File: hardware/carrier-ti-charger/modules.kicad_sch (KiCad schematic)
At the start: 30 parts, among them J10 J_ADS_MAIN ADSBee J5, J11 J_ADS_GNSS ADSBee J4, J6 J_ESP_A support, J7 J_ESP_B power/UART, J8 J_ESP_C I2C, J9 J_ESP_D support, U11 TPS259474LRPWR, U12 TPS259474LRPWR

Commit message: Consolidate bom.
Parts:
- C38, C39: value 100n 50V -> 100n 16V; footprint Capacitor_SMD:C_0603_1608Metric -> carrier:C_0402_1005Metric_NoSilk; LCSC C14663 -> C1525; MPN (none) -> CL05B104KO5NNNC
- R73, R75: value 5.36k -> 5.6k 1%; LCSC C2924137 -> C23189; MPN AR03BTCX5361A -> 0603WAF5601T5E; TCR 25 ppm/C -> 100 ppm/C; Tolerance 0.1% -> 1%
- R74, R76: value 1.5k -> 1.5k 1%; LCSC C281775 -> C25867; MPN RT0402BRD071K5L -> 0402WGF1501TCE; TCR 25 ppm/C -> 100 ppm/C; Tolerance 0.1% -> 1%
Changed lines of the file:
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@@
 			)
 		)
-		(property "Value" "1.5k"
+		(property "Value" "1.5k 1%"
 			(at 52.07 148.59 0)
 			(show_name no)
@@
 			)
 		)
-		(property "Description" "OVLO divider, 0.1%, 25 ppm/C, 62.5 mW, 50 V"
+		(property "Description" "OVLO divider bottom, U11, 1%, 100 ppm/C"
 			(at 54.61 147.32 0)
 			(hide yes)
@@
 			)
 		)
-		(property "LCSC" "C281775"
+		(property "LCSC" "C25867"
 			(at 54.61 147.32 0)
 			(hide yes)
@@
 			)
 		)
-		(property "MPN" "RT0402BRD071K5L"
+		(property "MPN" "0402WGF1501TCE"
 			(at 54.61 147.32 0)
 			(hide yes)
@@
 			)
 		)
-		(property "Tolerance" "0.1%"
+		(property "Tolerance" "1%"
 			(at 54.61 147.32 0)
 			(hide yes)
@@
 			)
 		)
-		(property "TCR" "25 ppm/C"
+		(property "TCR" "100 ppm/C"
 			(at 54.61 147.32 0)
 			(hide yes)
@@
 			)
 		)
-		(property "Value" "100n 50V"
+		(property "Value" "100n 16V"
 			(at 29.21 57.15 0)
 			(show_name no)
@@
 			)
 		)
-		(property "Footprint" "Capacitor_SMD:C_0603_1608Metric"
+		(property "Footprint" "carrier:C_0402_1005Metric_NoSilk"
 			(at 26.67 55.88 0)
 			(hide yes)
@@
 			)
 		)
-		(property "LCSC" "C14663"
+		(property "LCSC" "C1525"
+			(at 26.67 55.88 0)
+			(hide yes)
+			(show_name no)
+			(do_not_autoplace no)
+			(effects
+				(font
+					(size 1.27 1.27)
+				)
+			)
+		)
+		(property "MPN" "CL05B104KO5NNNC"
 			(at 26.67 55.88 0)
 			(hide yes)
@@
 			)
 		)
-		(property "Value" "5.36k"
+		(property "Value" "5.6k 1%"
 			(at 52.07 80.01 0)
 			(show_name no)
@@
 			)
 		)
-		(property "Description" "OVLO divider, 0.1%, 25 ppm/C, 100 mW, 75 V"
+		(property "Description" "OVLO divider top, U12, 1%, 100 ppm/C"
 			(at 54.61 78.74 0)
 			(hide yes)
@@
 			)
 		)
-		(property "LCSC" "C2924137"
+		(property "LCSC" "C23189"
 			(at 54.61 78.74 0)
 			(hide yes)
@@
 			)
 		)
-		(property "MPN" "AR03BTCX5361A"
+		(property "MPN" "0603WAF5601T5E"
 			(at 54.61 78.74 0)
 			(hide yes)
@@
 			)
 		)
-		(property "Tolerance" "0.1%"
+		(property "Tolerance" "1%"
 			(at 54.61 78.74 0)
 			(hide yes)
@@
 			)
 		)
-		(property "TCR" "25 ppm/C"
+		(property "TCR" "100 ppm/C"
 			(at 54.61 78.74 0)
 			(hide yes)
@@
 			)
 		)
-		(property "Value" "1.5k"
+		(property "Value" "1.5k 1%"
 			(at 52.07 87.63 0)
 			(show_name no)
@@
 			)
 		)
-		(property "Description" "OVLO divider, 0.1%, 25 ppm/C, 62.5 mW, 50 V"
+		(property "Description" "OVLO divider bottom, U12, 1%, 100 ppm/C"
 			(at 54.61 86.36 0)
 			(hide yes)
@@
 			)
 		)
-		(property "LCSC" "C281775"
+		(property "LCSC" "C25867"
 			(at 54.61 86.36 0)
 			(hide yes)
@@
 			)
 		)
-		(property "MPN" "RT0402BRD071K5L"
+		(property "MPN" "0402WGF1501TCE"
 			(at 54.61 86.36 0)
 			(hide yes)
@@
 			)
 		)
-		(property "Tolerance" "0.1%"
+		(property "Tolerance" "1%"
 			(at 54.61 86.36 0)
 			(hide yes)
@@
 			)
 		)
-		(property "TCR" "25 ppm/C"
+		(property "TCR" "100 ppm/C"
 			(at 54.61 86.36 0)
 			(hide yes)
@@
 			)
 		)
-		(property "Value" "100n 50V"
+		(property "Value" "100n 16V"
 			(at 29.21 118.11 0)
 			(show_name no)
@@
 			)
 		)
-		(property "Footprint" "Capacitor_SMD:C_0603_1608Metric"
+		(property "Footprint" "carrier:C_0402_1005Metric_NoSilk"
 			(at 26.67 116.84 0)
 			(hide yes)
@@
 			)
 		)
-		(property "LCSC" "C14663"
+		(property "LCSC" "C1525"
+			(at 26.67 116.84 0)
+			(hide yes)
+			(show_name no)
+			(do_not_autoplace no)
+			(effects
+				(font
+					(size 1.27 1.27)
+				)
+			)
+		)
+		(property "MPN" "CL05B104KO5NNNC"
 			(at 26.67 116.84 0)
 			(hide yes)
@@
 			)
 		)
-		(property "Value" "5.36k"
+		(property "Value" "5.6k 1%"
 			(at 52.07 140.97 0)
 			(show_name no)
@@
 			)
 		)
-		(property "Description" "OVLO divider, 0.1%, 25 ppm/C, 100 mW, 75 V"
+		(property "Description" "OVLO divider top, U11, 1%, 100 ppm/C"
 			(at 54.61 139.7 0)
 			(hide yes)
@@
 			)
 		)
-		(property "LCSC" "C2924137"
+		(property "LCSC" "C23189"
 			(at 54.61 139.7 0)
 			(hide yes)
@@
 			)
 		)
-		(property "MPN" "AR03BTCX5361A"
+		(property "MPN" "0603WAF5601T5E"
 			(at 54.61 139.7 0)
 			(hide yes)
@@
 			)
 		)
-		(property "Tolerance" "0.1%"
+		(property "Tolerance" "1%"
 			(at 54.61 139.7 0)
 			(hide yes)
@@
 			)
 		)
-		(property "TCR" "25 ppm/C"
+		(property "TCR" "100 ppm/C"
 			(at 54.61 139.7 0)
 			(hide yes)

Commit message: Polishing.
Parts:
- added J2: XIAO Plus power/UART/PWM, Connector_PinHeader_2.54mm:PinHeader_1x07_P2.54mm_Vertical, symbol Connector_Generic:Conn_01x07
- added J3: XIAO Plus I2C/spares, Connector_PinHeader_2.54mm:PinHeader_1x07_P2.54mm_Vertical, symbol Connector_Generic:Conn_01x07
- renumbered J7 to J1, J6 to J4, J11 to J5, J10 to J6, J9 to J8, J8 to J9, JP2 to JP3
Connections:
- net +ESP_3V3: now also J2.3 (Pin_3)
- net +ESP_5V: now also J2.1 (Pin_1)
- net BUZZ_PWM: now also J2.5 (Pin_5)
- net ESP_UART_RX: now also J2.6 (Pin_6)
- net ESP_UART_TX: now also J2.7 (Pin_7)
- net GND: now also J2.2 (Pin_2); no longer J1.4 (Pin_4), J4.4 (Pin_4)
- net I2C_SCL: now also J3.6 (Pin_6)
- net I2C_SDA: now also J3.5 (Pin_5)
- net XIAO_D0: now reaches J4.1 (Pin_1)
- net XIAO_D0: now also J3.1 (Pin_1)
- net XIAO_D1: now reaches J4.2 (Pin_2)
- net XIAO_D1: now also J3.2 (Pin_2)
- net XIAO_D2: now reaches J4.3 (Pin_3)
- net XIAO_D2: now also J3.3 (Pin_3)
- net XIAO_D6: now reaches J4.7 (Pin_7)
- net XIAO_D6: now also J3.7 (Pin_7)
- new net XIAO_D10: J1.4 (Pin_4), J2.4 (Pin_4)
- new net XIAO_D3: J3.4 (Pin_4), J4.4 (Pin_4)
- no-connect marks 21 -> 17

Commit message: Polishing.
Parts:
- R70, R71: value 1.65k -> 1.8k; LCSC C22845 -> C4177; MPN 0603WAF1651T5E -> 0603WAF1801T5E; Manufacturer (none) -> UNI-ROYAL; TCR (none) -> 100 ppm/°C; Tolerance (none) -> 1%
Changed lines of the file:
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@@
 			)
 		)
-		(property "Value" "1.65k"
+		(property "Value" "1.8k"
 			(at 67.31 148.59 0)
 			(show_name no)
@@
 			)
 		)
-		(property "Datasheet" ""
+		(property "Datasheet" "https://www.uni-royal.cn/en/images/userfile/file/1753752986c56505e6d9ab55c7.pdf"
 			(at 69.85 147.32 0)
 			(hide yes)
@@
 			)
 		)
-		(property "LCSC" "C22845"
-			(at 69.85 147.32 0)
-			(hide yes)
-			(show_name no)
-			(do_not_autoplace no)
-			(effects
-				(font
-					(size 1.27 1.27)
-				)
-			)
-		)
-		(property "MPN" "0603WAF1651T5E"
+		(property "LCSC" "C4177"
+			(at 69.85 147.32 0)
+			(hide yes)
+			(show_name no)
+			(do_not_autoplace no)
+			(effects
+				(font
+					(size 1.27 1.27)
+				)
+			)
+		)
+		(property "TCR" "100 ppm/°C"
+			(at 69.85 147.32 0)
+			(hide yes)
+			(show_name no)
+			(do_not_autoplace no)
+			(effects
+				(font
+					(size 1.27 1.27)
+				)
+			)
+		)
+		(property "Tolerance" "1%"
+			(at 69.85 147.32 0)
+			(hide yes)
+			(show_name no)
+			(do_not_autoplace no)
+			(effects
+				(font
+					(size 1.27 1.27)
+				)
+			)
+		)
+		(property "Manufacturer" "UNI-ROYAL"
+			(at 69.85 147.32 0)
+			(hide yes)
+			(show_name no)
+			(do_not_autoplace no)
+			(effects
+				(font
+					(size 1.27 1.27)
+				)
+			)
+		)
+		(property "MPN" "0603WAF1801T5E"
 			(at 69.85 147.32 0)
 			(hide yes)
@@
 			)
 		)
-		(property "Value" "1.65k"
+		(property "Value" "1.8k"
 			(at 67.31 87.63 0)
 			(show_name no)
@@
 			)
 		)
-		(property "Datasheet" ""
+		(property "Datasheet" "https://www.uni-royal.cn/en/images/userfile/file/1753752986c56505e6d9ab55c7.pdf"
 			(at 69.85 86.36 0)
 			(hide yes)
@@
 			)
 		)
-		(property "LCSC" "C22845"
-			(at 69.85 86.36 0)
-			(hide yes)
-			(show_name no)
-			(do_not_autoplace no)
-			(effects
-				(font
-					(size 1.27 1.27)
-				)
-			)
-		)
-		(property "MPN" "0603WAF1651T5E"
-			(at 69.85 86.36 0)
-			(hide yes)
+		(property "LCSC" "C4177"
+			(at 69.85 86.36 0)
+			(hide yes)
+			(show_name no)
+			(do_not_autoplace no)
+			(effects
+				(font
+					(size 1.27 1.27)
+				)
+			)
+		)
+		(property "TCR" "100 ppm/°C"
+			(at 69.85 86.36 0)
+			(hide yes)
+			(show_name no)
+			(do_not_autoplace no)
+			(effects
+				(font
+					(size 1.27 1.27)
+				)
+			)
+		)
+		(property "Tolerance" "1%"
+			(at 69.85 86.36 0)
+			(hide yes)
+			(show_name no)
+			(do_not_autoplace no)
+			(effects
+				(font
+					(size 1.27 1.27)
+				)
+			)
+		)
+		(property "Manufacturer" "UNI-ROYAL"
+			(at 69.85 86.36 0)
+			(hide yes)
+			(show_name no)
+			(do_not_autoplace no)
+			(effects
+				(font
+					(size 1.27 1.27)
+				)
+			)
+		)
+		(property "MPN" "0603WAF1801T5E"
+			(at 69.85 86.36 0)
+			(hide yes)

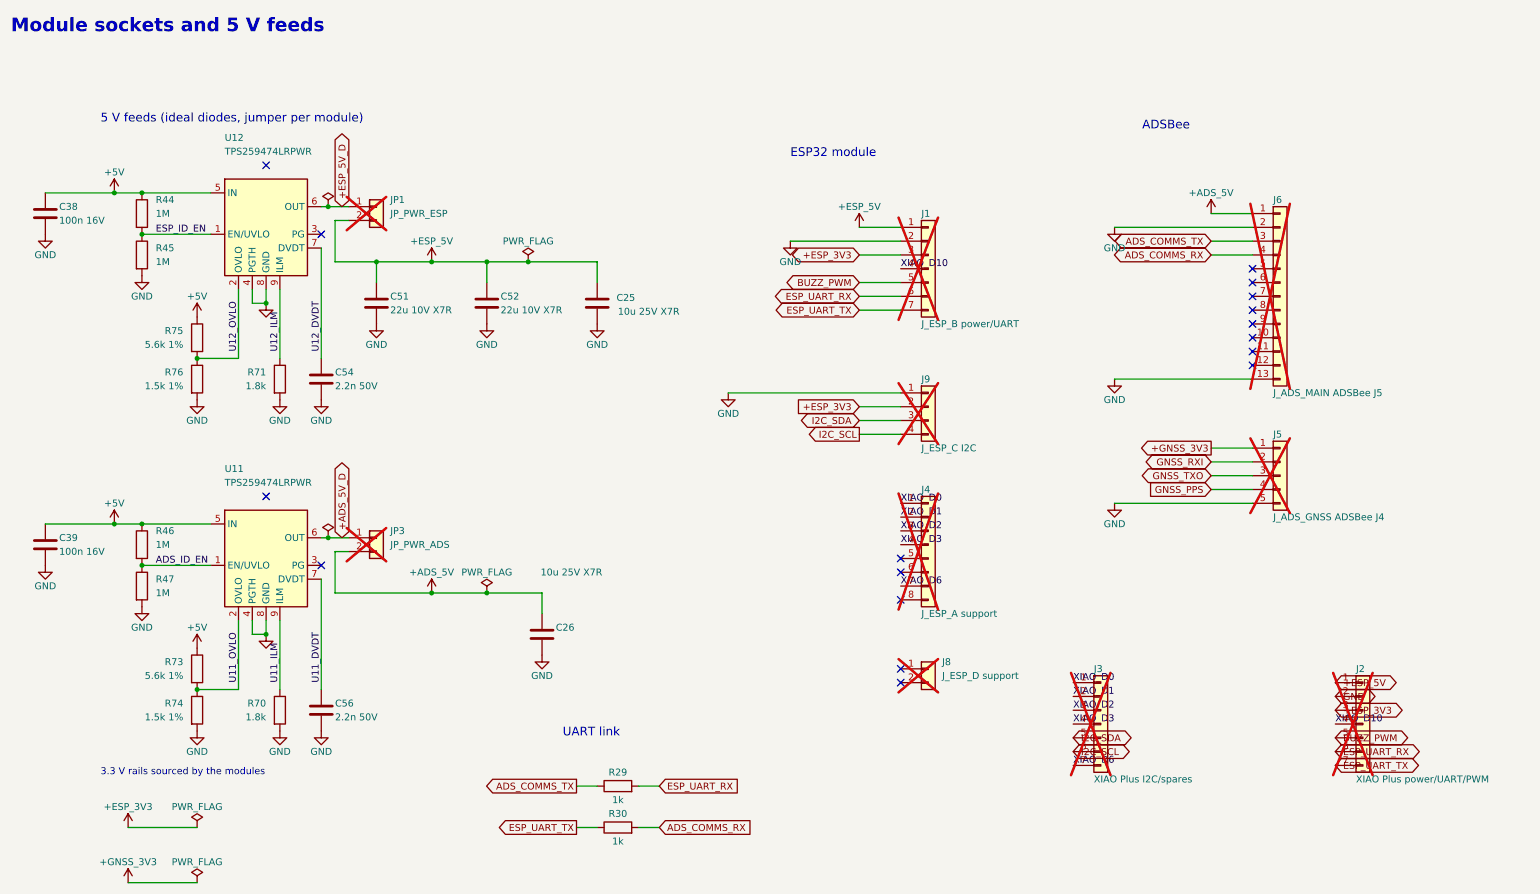
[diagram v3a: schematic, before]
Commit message: Consolidate BOM, add GNSS listen to ESP.
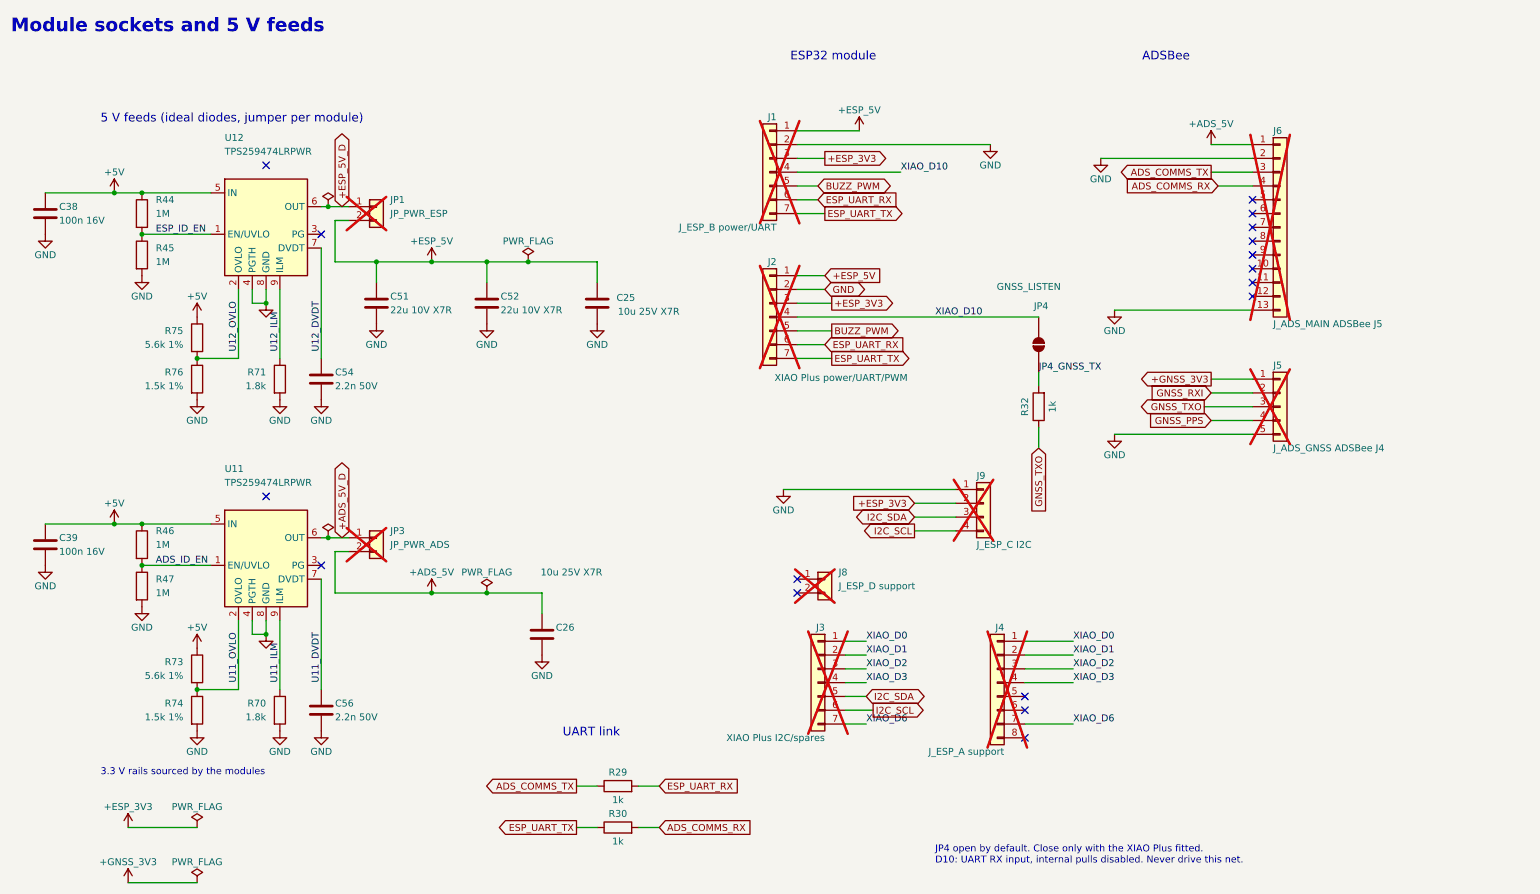
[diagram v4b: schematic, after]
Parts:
- added JP4: GNSS_LISTEN, Jumper:SolderJumper-2_P1.3mm_Open_RoundedPad1.0x1.5mm, symbol Jumper:SolderJumper_2_Open
- added R32: 1k, Resistor_SMD:R_0603_1608Metric, symbol Device:R
- C38, C39: footprint carrier:C_0402_1005Metric_NoSilk -> Mark:C_0402_1005Metric_NoSilk
- R74, R76: footprint carrier:R_0402_1005Metric_NoSilk -> Mark:R_0402_1005Metric_NoSilk
- U11, U12: footprint carrier:VQFN-10_L2.0-W2.0-P0.45-HR_LM73100 -> Mark:VQFN-10_L2.0-W2.0-P0.45-HR_LM73100; symbol carrier:TPS259474LRPW -> Mark:TPS259474LRPW
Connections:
- net GNSS_TXO: now also R32.1
- net XIAO_D10: now also JP4.2 (B)
- new net JP4_GNSS_TX: JP4.1 (A), R32.2
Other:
- note added: "JP4 open by default. Close only with the XIAO Plus fitted. D10: UART RX input, internal pulls disabled. Never drive this net."
- moved on the sheet: J1, J2, J3, J4, J5, J6, J8, J9
